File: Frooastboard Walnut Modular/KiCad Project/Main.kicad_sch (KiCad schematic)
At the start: 322 parts, among them J12 Conn_01x16, J13 Conn_01x06, J14 Conn_01x06, J15 F Row, J16 F Row USB, J17 Numpad, M2 Frooastboard_MM2040

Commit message: almost finish schematic
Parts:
- removed D? (x102): RGB_LED_6_Pin, Frooastboard Footprints:Everlight 99-235, symbol Frooastboard Symbols:RGB_LED_6_Pin
- removed J12: Conn_01x16, symbol Connector_Generic:Conn_01x16
- removed J13, J14: Conn_01x06, symbol Connector_Generic:Conn_01x06
- removed J?: Conn_01x16_Male, symbol Connector:Conn_01x16_Male
- removed J?: Conn_01x15_Male, symbol Connector:Conn_01x15_Male
- removed J? (x2): Conn_01x06_Male, symbol Connector:Conn_01x06_Male
- removed R23, R24: 27R, Resistor_SMD:R_0805_2012Metric, symbol Device:R_Small
- gave numbers to parts that had none: 5
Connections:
- net CS1: now also M2.13 (CS1)
- net CS10: now also M2.22 (CS10)
- net CS11: now also M2.23 (CS11)
- net CS12: now also M2.24 (CS12)
- net CS13: now also M2.25 (CS13)
- net CS14: now also M2.26 (CS14)
- net CS15: now also M2.27 (CS15)
- net CS16: now also M2.28 (CS16)
- net CS2: now also M2.14 (CS2)
- net CS3: now also M2.15 (CS3)
- net CS4: now also M2.16 (CS4)
- net CS5: now also M2.17 (CS5)
- net CS6: now also M2.18 (CS6)
- net CS7: now also M2.19 (CS7)
- net CS8: now also M2.20 (CS8)
- net CS9: now also M2.21 (CS9)
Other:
- moved on the sheet: C38, D113, D114, D115, D116, D117, D122, D123, D124, D125, D126, D127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

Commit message: do some stuff
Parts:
- added MX?: Enter, symbol MX_Alps_Hybrid:MX-NoLED
- added MX?: Left Shift, symbol MX_Alps_Hybrid:MX-NoLED
- added MX?: \, symbol MX_Alps_Hybrid:MX-NoLED
- MX100: value MX-NoLED -> Home
- MX101: value MX-NoLED -> End
- MX102: value MX-NoLED -> 7
- MX103: value MX-NoLED -> U
- MX104: value MX-NoLED -> J
- MX105: value MX-NoLED -> N
- MX106: value MX-NoLED -> Right Control
- MX107: value MX-NoLED -> Right
- MX108: value MX-NoLED -> Down
- MX109: value MX-NoLED -> Page Up
- MX110: value MX-NoLED -> Page Down
- MX39: value MX-NoLED -> Escape
- MX40: value MX-NoLED -> Tab
- MX41: value MX-NoLED -> Caps Lock
- MX42: value MX-NoLED -> Left Shift
- MX43: value MX-NoLED -> Left Control
- MX44: value MX-NoLED -> 8
- MX45: value MX-NoLED -> I
- MX46: value MX-NoLED -> K
- MX47: value MX-NoLED -> M
- MX48: value MX-NoLED -> 1
- MX49: value MX-NoLED -> Q
- MX50: value MX-NoLED -> A
- MX51, MX82: value MX-NoLED -> \
- MX52: value MX-NoLED -> Left GUI
- MX53: value MX-NoLED -> 9
- MX54: value MX-NoLED -> O
- MX55: value MX-NoLED -> L
- MX56: value MX-NoLED -> ,
- MX57: value MX-NoLED -> 2
- MX58: value MX-NoLED -> W
- MX59: value MX-NoLED -> S
- MX60: value MX-NoLED -> Z
- MX61: value MX-NoLED -> Left Alt
- MX62: value MX-NoLED -> 0
- MX63: value MX-NoLED -> P
- MX64: value MX-NoLED -> ;
- MX65: value MX-NoLED -> .
- MX66: value MX-NoLED -> 3
- MX67: value MX-NoLED -> E
- MX68: value MX-NoLED -> D
- MX69: value MX-NoLED -> X
- MX70: value MX-NoLED -> Space
- MX71: value MX-NoLED -> -
- MX72: value MX-NoLED -> [
- MX73: value MX-NoLED -> '
- MX74: value MX-NoLED -> /
- MX75: value MX-NoLED -> 4
- MX76: value MX-NoLED -> R
- MX77: value MX-NoLED -> F
- MX78: value MX-NoLED -> C
- MX79: value MX-NoLED -> Right Alt
- MX80: value MX-NoLED -> =
- MX81: value MX-NoLED -> ]
- MX83: value MX-NoLED -> Right Shift
- MX84: value MX-NoLED -> 5
- MX85: value MX-NoLED -> T
- MX86: value MX-NoLED -> G
- MX87: value MX-NoLED -> V
- MX88: value MX-NoLED -> Function
- MX89: value MX-NoLED -> Backspace
- MX90: value MX-NoLED -> Enter
- MX91: value MX-NoLED -> Insert
- MX92: value MX-NoLED -> Delete
- MX93: value MX-NoLED -> 6
- MX94: value MX-NoLED -> Y
- MX95: value MX-NoLED -> H
- MX96: value MX-NoLED -> B
- MX97: value MX-NoLED -> Menu
- MX98: value MX-NoLED -> Left
- MX99: value MX-NoLED -> Up
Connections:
- net COL0: now also MX?.1 (COL)
- net COL4: now also MX?.1 (COL)
- net COL5: now also MX?.1 (COL)
- net at D116.2 (A), MX42.2 (ROW): now also MX?.2 (ROW)
- net at D184.2 (A), MX90.2 (ROW): now also MX?.2 (ROW)
- net at D172.2 (A), MX82.2 (ROW): now also MX?.2 (ROW)

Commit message: before nrf52810
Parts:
- gave numbers to parts that had none: 3
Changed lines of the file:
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@@
   (symbol (lib_id "MX_Alps_Hybrid:MX-NoLED") (at 163.83 204.47 0) (unit 1)
     (in_bom yes) (on_board yes) (fields_autoplaced)
-    (property "Reference" "MX?" (id 0) (at 164.7156 198.12 0)
+    (property "Reference" "MX113" (id 0) (at 164.7156 198.12 0)
       (effects (font (size 1.524 1.524)))
     )
@@
   (symbol (lib_id "MX_Alps_Hybrid:MX-NoLED") (at 59.69 234.95 0) (unit 1)
     (in_bom yes) (on_board yes) (fields_autoplaced)
-    (property "Reference" "MX?" (id 0) (at 60.5756 228.6 0)
+    (property "Reference" "MX111" (id 0) (at 60.5756 228.6 0)
       (effects (font (size 1.524 1.524)))
     )
@@
   (symbol (lib_id "MX_Alps_Hybrid:MX-NoLED") (at 144.78 220.98 0) (unit 1)
     (in_bom yes) (on_board yes) (fields_autoplaced)
-    (property "Reference" "MX?" (id 0) (at 145.6656 214.63 0)
-      (effects (font (size 1.524 1.524)))
-    )
+    (property "Reference" "MX112" (id 0) (at 145.6656 214.63 0)
+      (effects (font (size 1.524 1.524)))
+    )

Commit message: some new stuff
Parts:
- removed D111: RGB_LED_6_Pin, Frooastboard Footprints:Everlight 99-235, symbol Frooastboard Symbols:RGB_LED_6_Pin
- added D5: Caps Lock Indicator, LED_SMD:LED_0805_2012Metric, symbol Device:LED
- C38: footprint (none) -> Capacitor_SMD:C_0805_2012Metric
- D113, D114, D115, D116, D117, D122, D123, D124, D125, D126, D127, D128, D129, D130, D131, D132, D133, D134, D139, D140, D141, D142, D143, D144, D145, D146, D147, D152, D153, D154, D155, D156, D157, D158, D159, D160, D165, D166, D167, D168, D169, D170, D171, D172, D173, D174, D175, D176, D177, D178, D183, D184, D185, D186, D187, D188, D189, D190, D191, D195, D196, D197, D198, D199, D200, D201, D202, D203, D204, D205, D206, D207: footprint (none) -> Diode_SMD:D_0805_2012Metric
- J10, J8: footprint (none) -> Frooastboard Footprints:PinHeader_1x16_P1.27mm_Vertical
- J11, J9: footprint (none) -> Frooastboard Footprints:PinHeader_1x06_P1.27mm_Vertical
- J15: footprint (none) -> Frooastboard Footprints:PinHeader_1x10_P1.27mm_Vertical
- J16: footprint (none) -> Frooastboard Footprints:PinHeader_1x04_P1.27mm_Vertical
- J17: footprint (none) -> Frooastboard Footprints:PinHeader_1x13_P1.27mm_Vertical
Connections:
- net CS2: now also D5.2 (A)
- net SW4: now also D5.1 (K)

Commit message: asign pieces
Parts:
- MX100, MX101, MX102, MX103, MX104, MX105, MX107, MX108, MX109, MX110, MX39, MX44, MX45, MX46, MX47, MX48, MX49, MX50, MX51, MX53, MX54, MX55, MX56, MX57, MX58, MX59, MX60, MX62, MX63, MX64, MX65, MX66, MX67, MX68, MX69, MX71, MX72, MX73, MX74, MX75, MX76, MX77, MX78, MX80, MX81, MX82, MX84, MX85, MX86, MX87, MX91, MX92, MX93, MX94, MX95, MX96, MX98, MX99: footprint (none) -> MX_Only:MXOnly-1U-NoLED
- MX106, MX42, MX43, MX52, MX61, MX79, MX88, MX97: footprint (none) -> MX_Only:MXOnly-1.25U-NoLED
- MX111, MX113: footprint (none) -> MX_Only:MXOnly-2.25U-NoLED
- MX112, MX40: footprint (none) -> MX_Only:MXOnly-1.5U-NoLED
- MX41: footprint (none) -> MX_Only:MXOnly-1.75U
- MX70: footprint (none) -> MX_Only:MXOnly-6.25U-ReversedStabilizers-NoLED
- MX83: footprint (none) -> MX_Only:MXOnly-2.75U-NoLED
- MX89: footprint (none) -> MX_Only:MXOnly-2U-NoLED
- MX90: footprint (none) -> MX_Only:MXOnly-ISO-ROTATED-NoLED-NoStabilizers
- R25: footprint (none) -> Resistor_SMD:R_0805_2012Metric

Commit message: more footprint changes
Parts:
- J10, J8: footprint Frooastboard Footprints:PinHeader_1x16_P1.27mm_Vertical -> Connector_PinHeader_1.27mm:PinHeader_1x16_P1.27mm_Vertical
- J11, J9: footprint Frooastboard Footprints:PinHeader_1x06_P1.27mm_Vertical -> Connector_PinHeader_1.27mm:PinHeader_1x06_P1.27mm_Vertical
- J15: footprint Frooastboard Footprints:PinHeader_1x10_P1.27mm_Vertical -> Connector_PinHeader_1.27mm:PinHeader_1x10_P1.27mm_Vertical
- J16: footprint Frooastboard Footprints:PinHeader_1x04_P1.27mm_Vertical -> Connector_PinHeader_1.27mm:PinHeader_1x04_P1.27mm_Vertical
- J17: footprint Frooastboard Footprints:PinHeader_1x13_P1.27mm_Vertical -> Connector_PinHeader_1.27mm:PinHeader_1x13_P1.27mm_Vertical

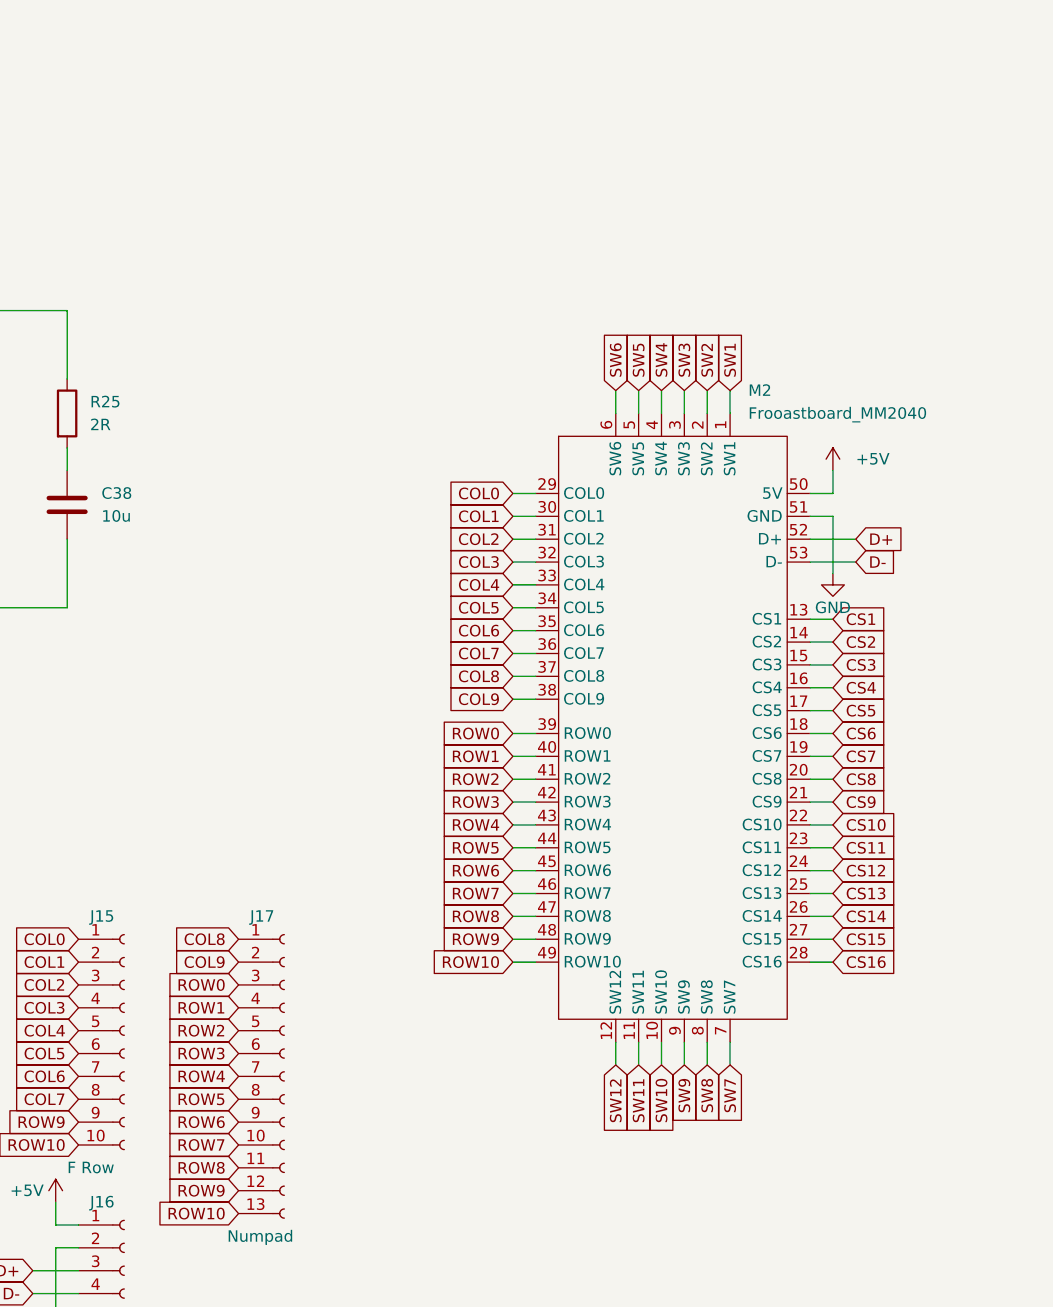
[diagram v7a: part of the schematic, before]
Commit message: import mm2040
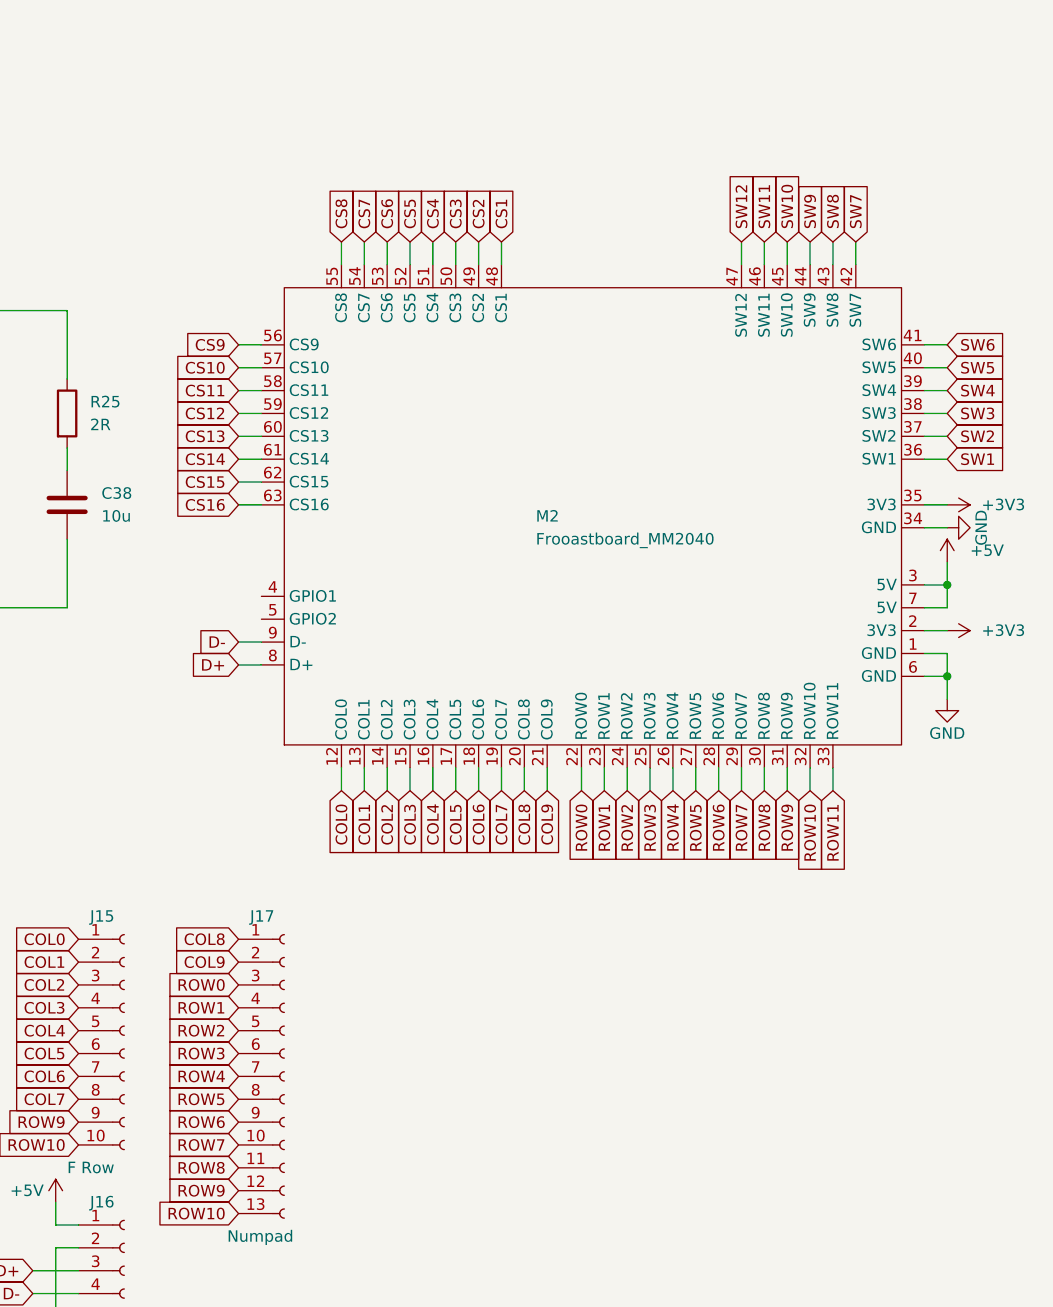
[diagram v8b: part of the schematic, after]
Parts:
- M2: footprint (none) -> Frooastboard Footprints:MM2040
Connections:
- net +5V: now also M2.3 (5V), M2.7 (5V); no longer M2.50 (5V)
- net COL0: now also M2.12 (COL0); no longer M2.29 (COL0)
- net COL1: now also M2.13 (COL1); no longer M2.30 (COL1)
- net COL2: now also M2.14 (COL2); no longer M2.31 (COL2)
- net COL3: now also M2.15 (COL3); no longer M2.32 (COL3)
- net COL4: now also M2.16 (COL4); no longer M2.33 (COL4)
- net COL5: now also M2.17 (COL5); no longer M2.34 (COL5)
- net COL6: now also M2.18 (COL6); no longer M2.35 (COL6)
- net COL7: now also M2.19 (COL7); no longer M2.36 (COL7)
- net COL8: now also M2.20 (COL8); no longer M2.37 (COL8)
- net COL9: now also M2.21 (COL9); no longer M2.38 (COL9)
- net CS1: now also M2.48 (CS1); no longer M2.13 (CS1)
- net CS10: now also M2.57 (CS10); no longer M2.22 (CS10)
- net CS11: now also M2.58 (CS11); no longer M2.23 (CS11)
- net CS12: now also M2.59 (CS12); no longer M2.24 (CS12)
- net CS13: now also M2.60 (CS13); no longer M2.25 (CS13)
- net CS14: now also M2.61 (CS14); no longer M2.26 (CS14)
- net CS15: now also M2.62 (CS15); no longer M2.27 (CS15)
- net CS16: now also M2.63 (CS16); no longer M2.28 (CS16)
- net CS2: now also M2.49 (CS2); no longer M2.14 (CS2)
- net CS3: now also M2.50 (CS3); no longer M2.15 (CS3)
- net CS4: now also M2.51 (CS4); no longer M2.16 (CS4)
- net CS5: now also M2.52 (CS5); no longer M2.17 (CS5)
- net CS6: now also M2.53 (CS6); no longer M2.18 (CS6)
- net CS7: now also M2.54 (CS7); no longer M2.19 (CS7)
- net CS8: now also M2.55 (CS8); no longer M2.20 (CS8)
- net CS9: now also M2.56 (CS9); no longer M2.21 (CS9)
- net D+: now also M2.8 (D+); no longer M2.52 (D+)
- net D-: now also M2.9 (D-); no longer M2.53 (D-)
- net GND: now also M2.1 (GND), M2.34 (GND), M2.6 (GND); no longer M2.51 (GND)
- net ROW0: now also M2.22 (ROW0); no longer M2.39 (ROW0)
- net ROW1: now also M2.23 (ROW1); no longer M2.40 (ROW1)
- net ROW10: now also M2.32 (ROW10); no longer M2.49 (ROW10)
- net ROW2: now also M2.24 (ROW2); no longer M2.41 (ROW2)
- net ROW3: now also M2.25 (ROW3); no longer M2.42 (ROW3)
- net ROW4: now also M2.26 (ROW4); no longer M2.43 (ROW4)
- net ROW5: now also M2.27 (ROW5); no longer M2.44 (ROW5)
- net ROW6: now also M2.28 (ROW6); no longer M2.45 (ROW6)
- net ROW7: now also M2.29 (ROW7); no longer M2.46 (ROW7)
- net ROW8: now also M2.30 (ROW8); no longer M2.47 (ROW8)
- net ROW9: now also M2.31 (ROW9); no longer M2.48 (ROW9)
- net SW1: now also M2.36 (SW1); no longer M2.1 (SW1)
- net SW10: now also M2.45 (SW10); no longer M2.10 (SW10)
- net SW11: now also M2.46 (SW11); no longer M2.11 (SW11)
- net SW12: now also M2.47 (SW12); no longer M2.12 (SW12)
- net SW2: now also M2.37 (SW2); no longer M2.2 (SW2)
- net SW3: now also M2.38 (SW3); no longer M2.3 (SW3)
- net SW4: now also M2.39 (SW4); no longer M2.4 (SW4)
- net SW5: now also M2.40 (SW5); no longer M2.5 (SW5)
- net SW6: now also M2.41 (SW6); no longer M2.6 (SW6)
- net SW7: now also M2.42 (SW7); no longer M2.7 (SW7)
- net SW8: now also M2.43 (SW8); no longer M2.8 (SW8)
- net SW9: now also M2.44 (SW9); no longer M2.9 (SW9)
- new net +3V3: M2.2 (3V3), M2.35 (3V3)
- new net ROW11: M2.33 (ROW11)
